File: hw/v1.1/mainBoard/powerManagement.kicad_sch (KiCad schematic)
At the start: 31 parts, among them J10 BAT+, J9 BAT-, Q10 AO3401A, Q11 2N7002, Q12 AO3401A, Q13 2N7002, Q5 AO3401A, Q6 2N7002, Q9 AO3401A, U10 AP1603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

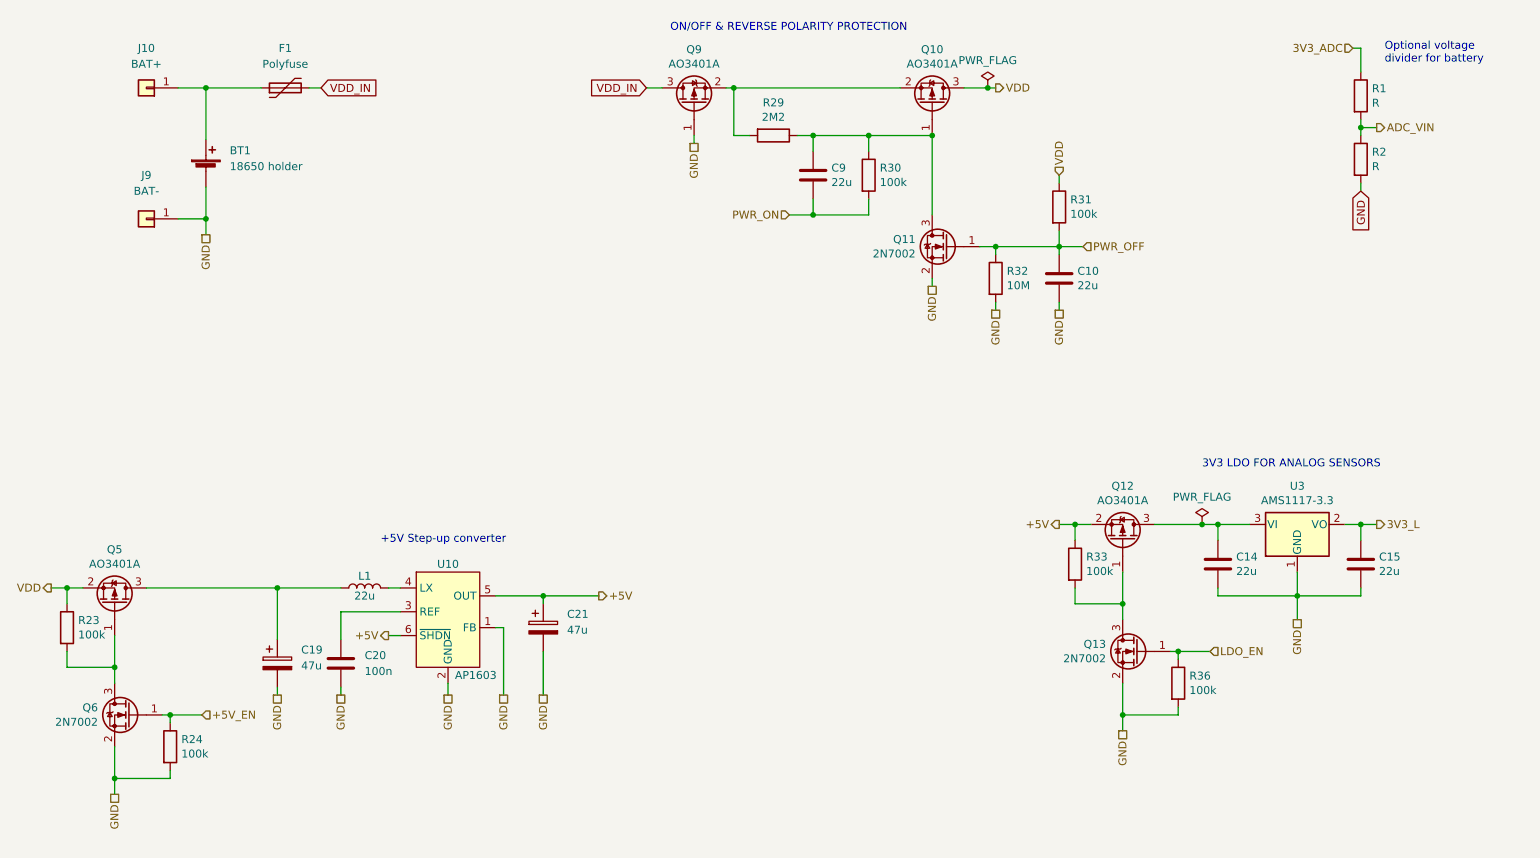
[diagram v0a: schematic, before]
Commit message: Beautify schematics in KiCad
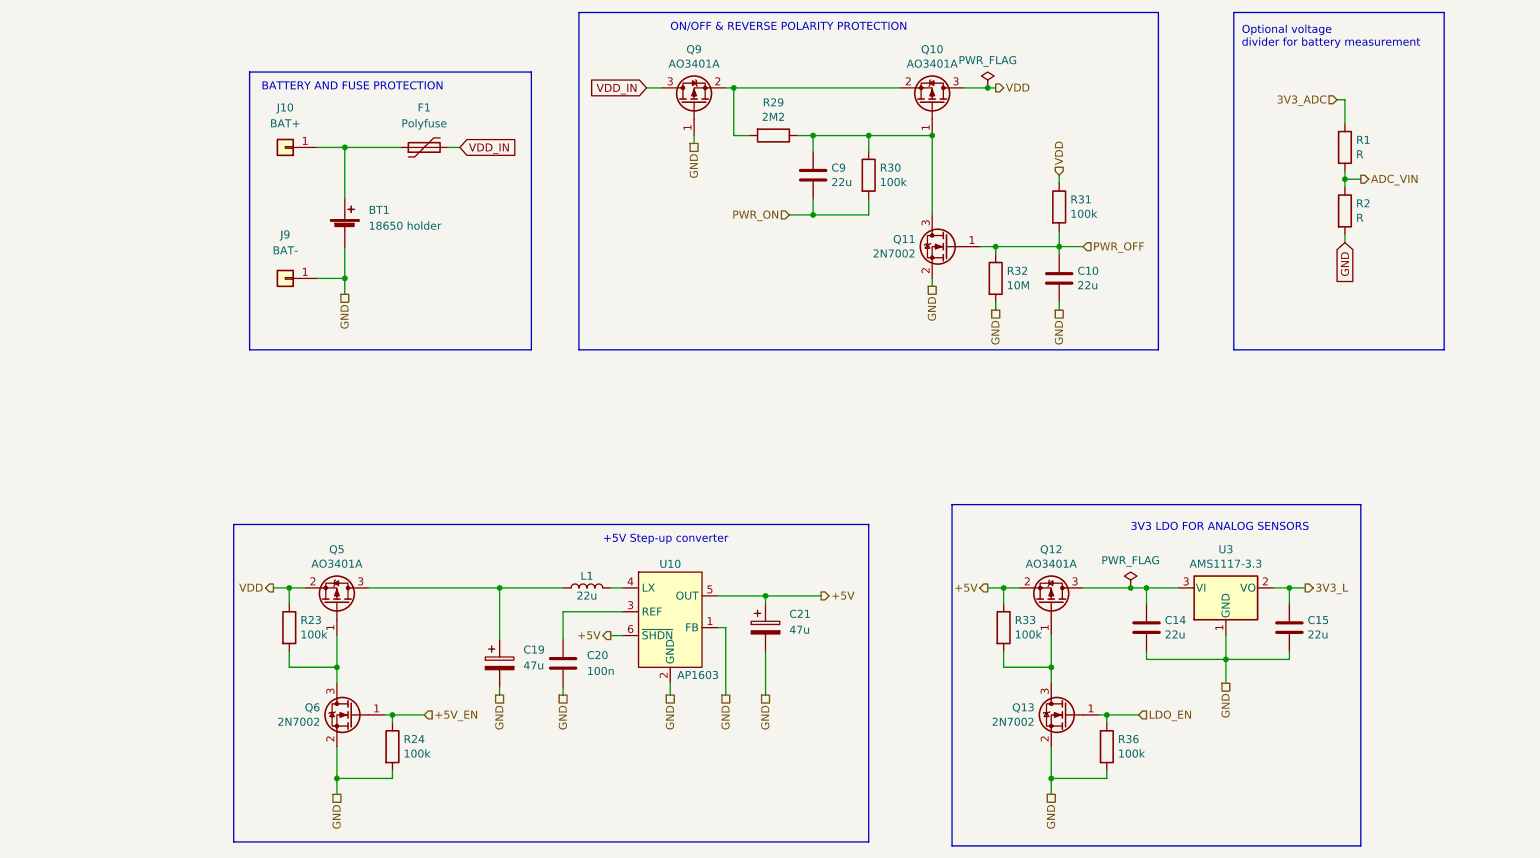
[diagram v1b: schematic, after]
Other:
- note added: "BATTERY AND FUSE PROTECTION"
- note added: "Optional voltage divider for battery measurement"
- note removed: "Optional voltage divider for battery"
- company: (none) -> Martin Kousal
- moved on the sheet: BT1, C14, C15, C19, C20, C21, F1, J10, J9, L1, Q12, Q13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
